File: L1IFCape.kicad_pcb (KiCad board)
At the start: 4 copper layers, 86.4 x 54.6 mm, 92 parts, among them J1 RF_Shield_One_Piece, J2 SMA, J3 MMCX, P8 BeagleBone_Black_Header, P9 BeagleBone_Black_Header, U1 24CS256, U2 MAX2769BETI+T, U3 MAX31343ETAY+T, U4 TPS717285DCK, U5 TPS717285DCK, X1 SIT5156, X2 QPQ1060

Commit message: Made Assembly Drawing
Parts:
- TP5: value ~{SHDN} -> BBClk

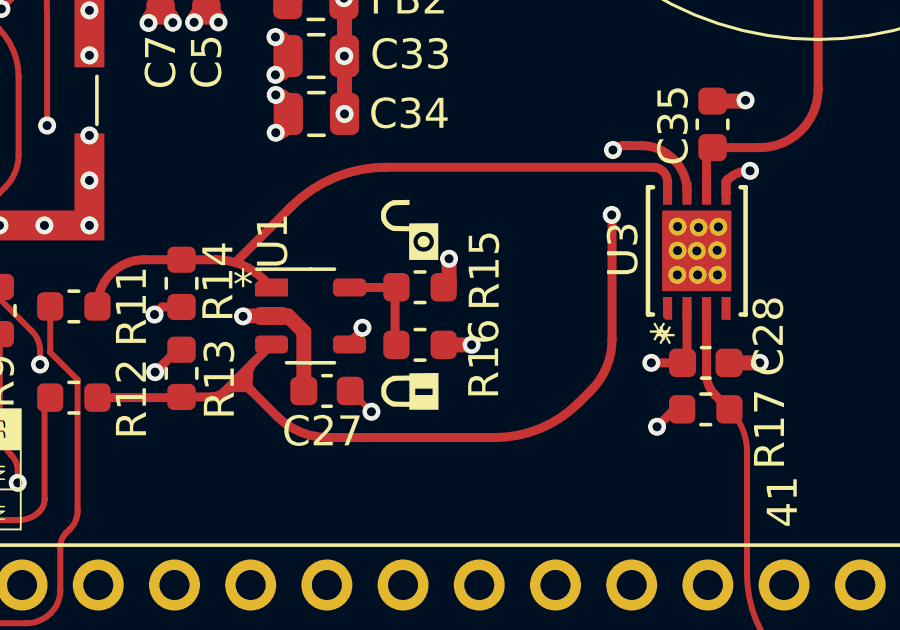
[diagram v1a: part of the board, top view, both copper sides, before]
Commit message: Added schematic to the back and cleaned up some schematic issues
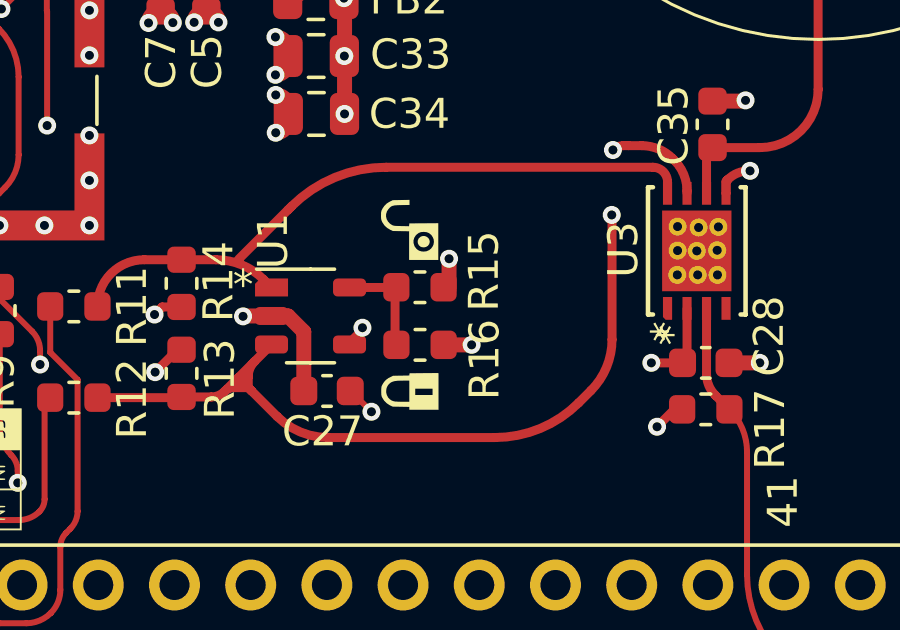
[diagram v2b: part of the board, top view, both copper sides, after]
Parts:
- added G***: LOGO, L1IF:L1IFCape-C3_SCH, F.Cu at (151.2, 71.6)
- C19: value NL -> 470 pF
- C29, C30: value NL -> 10 nF
- R16, R2, R5: value NL -> 0
- turned R15 to 180 degrees
- turned R16 to 0 degrees
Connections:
- R15 pad 1: Net-(U1-WP) -> GND
- R15 pad 2: GND -> Net-(U1-WP)
- R16 pad 1: +3V3 -> Net-(U1-WP)
- R16 pad 2: Net-(U1-WP) -> +3V3
